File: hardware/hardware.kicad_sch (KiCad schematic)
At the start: 0 parts

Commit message: Prel. pin assignments for base station
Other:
- sheet GNSS ports: added 3V3, GND, RXD, SCL, SDA, TXD; removed none
- sheet Heltecv3 ports: added 3V3, 5V, GND, SCL, SDA, UART_RX, UART_TX; removed none

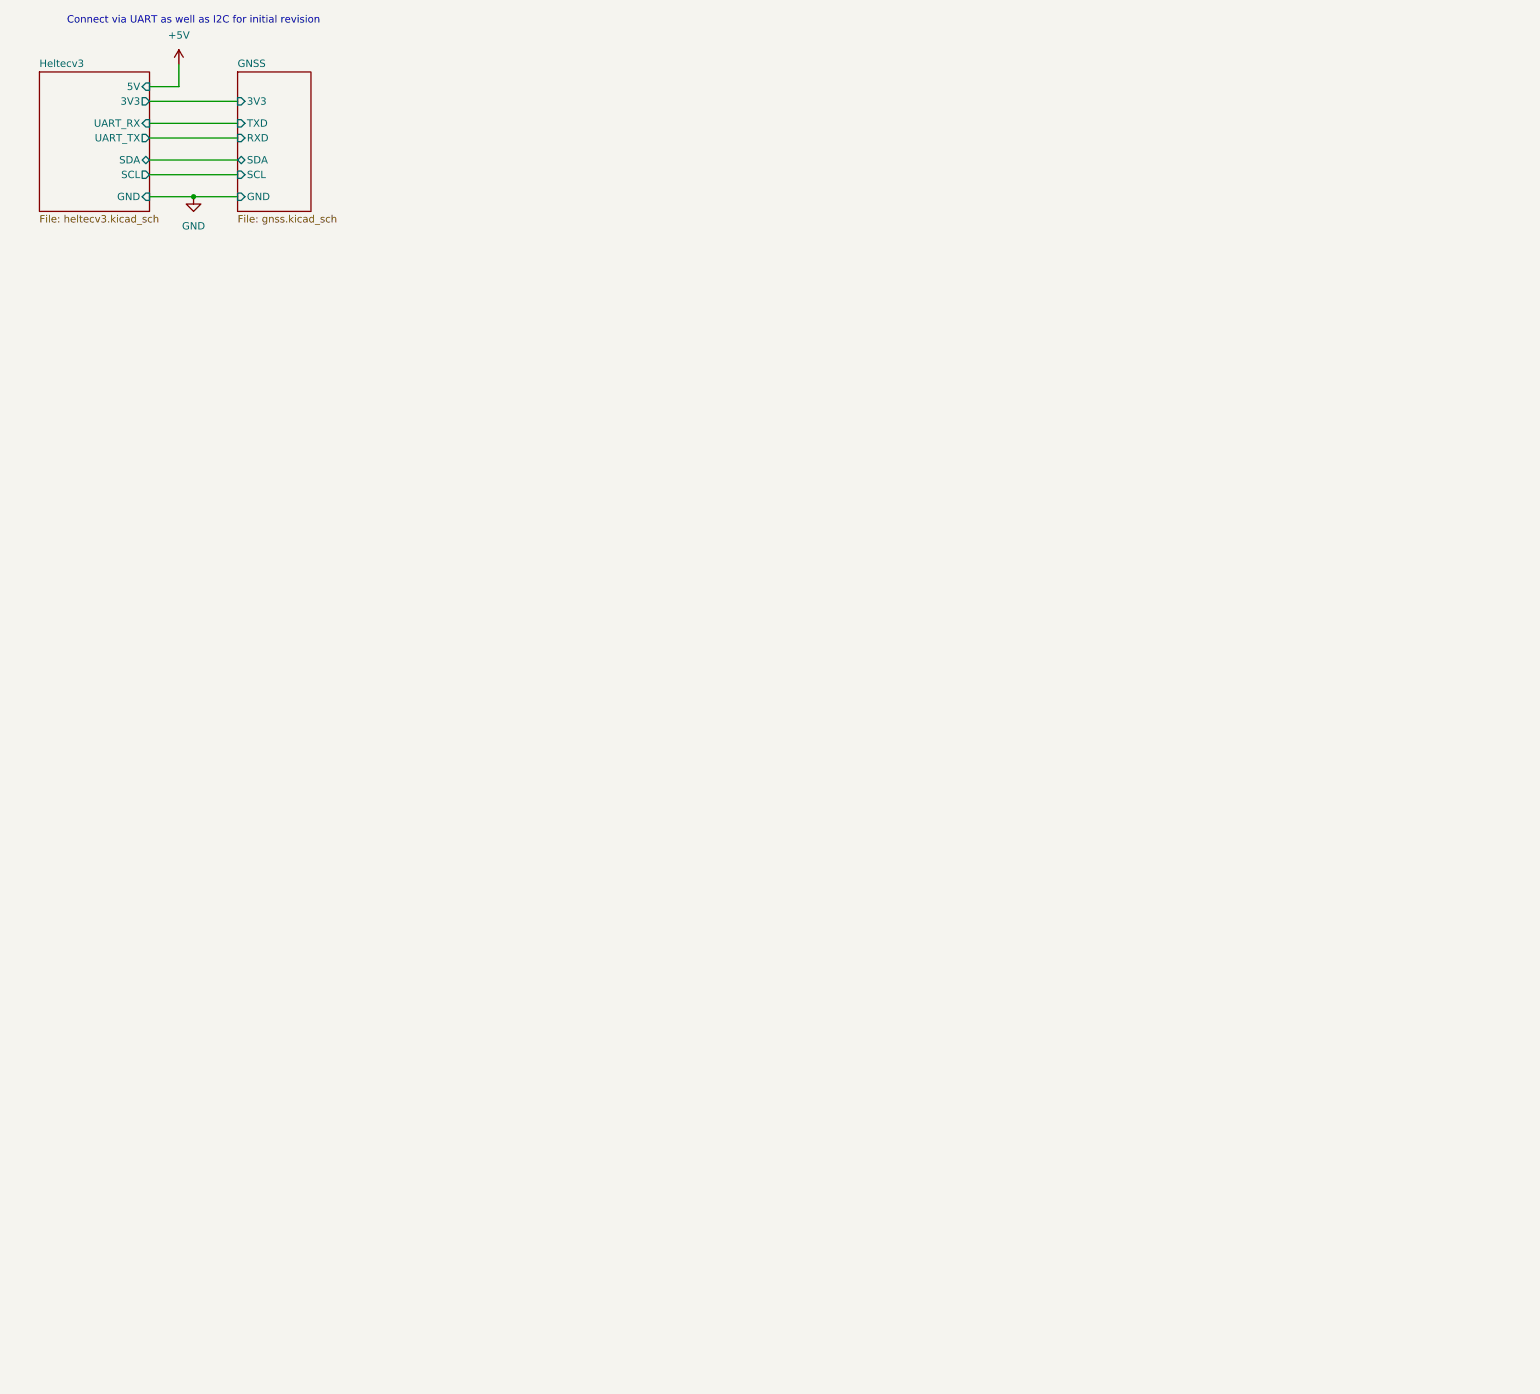
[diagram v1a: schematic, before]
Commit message: added footprints, symbols and so on. also added esp32 to main schematic
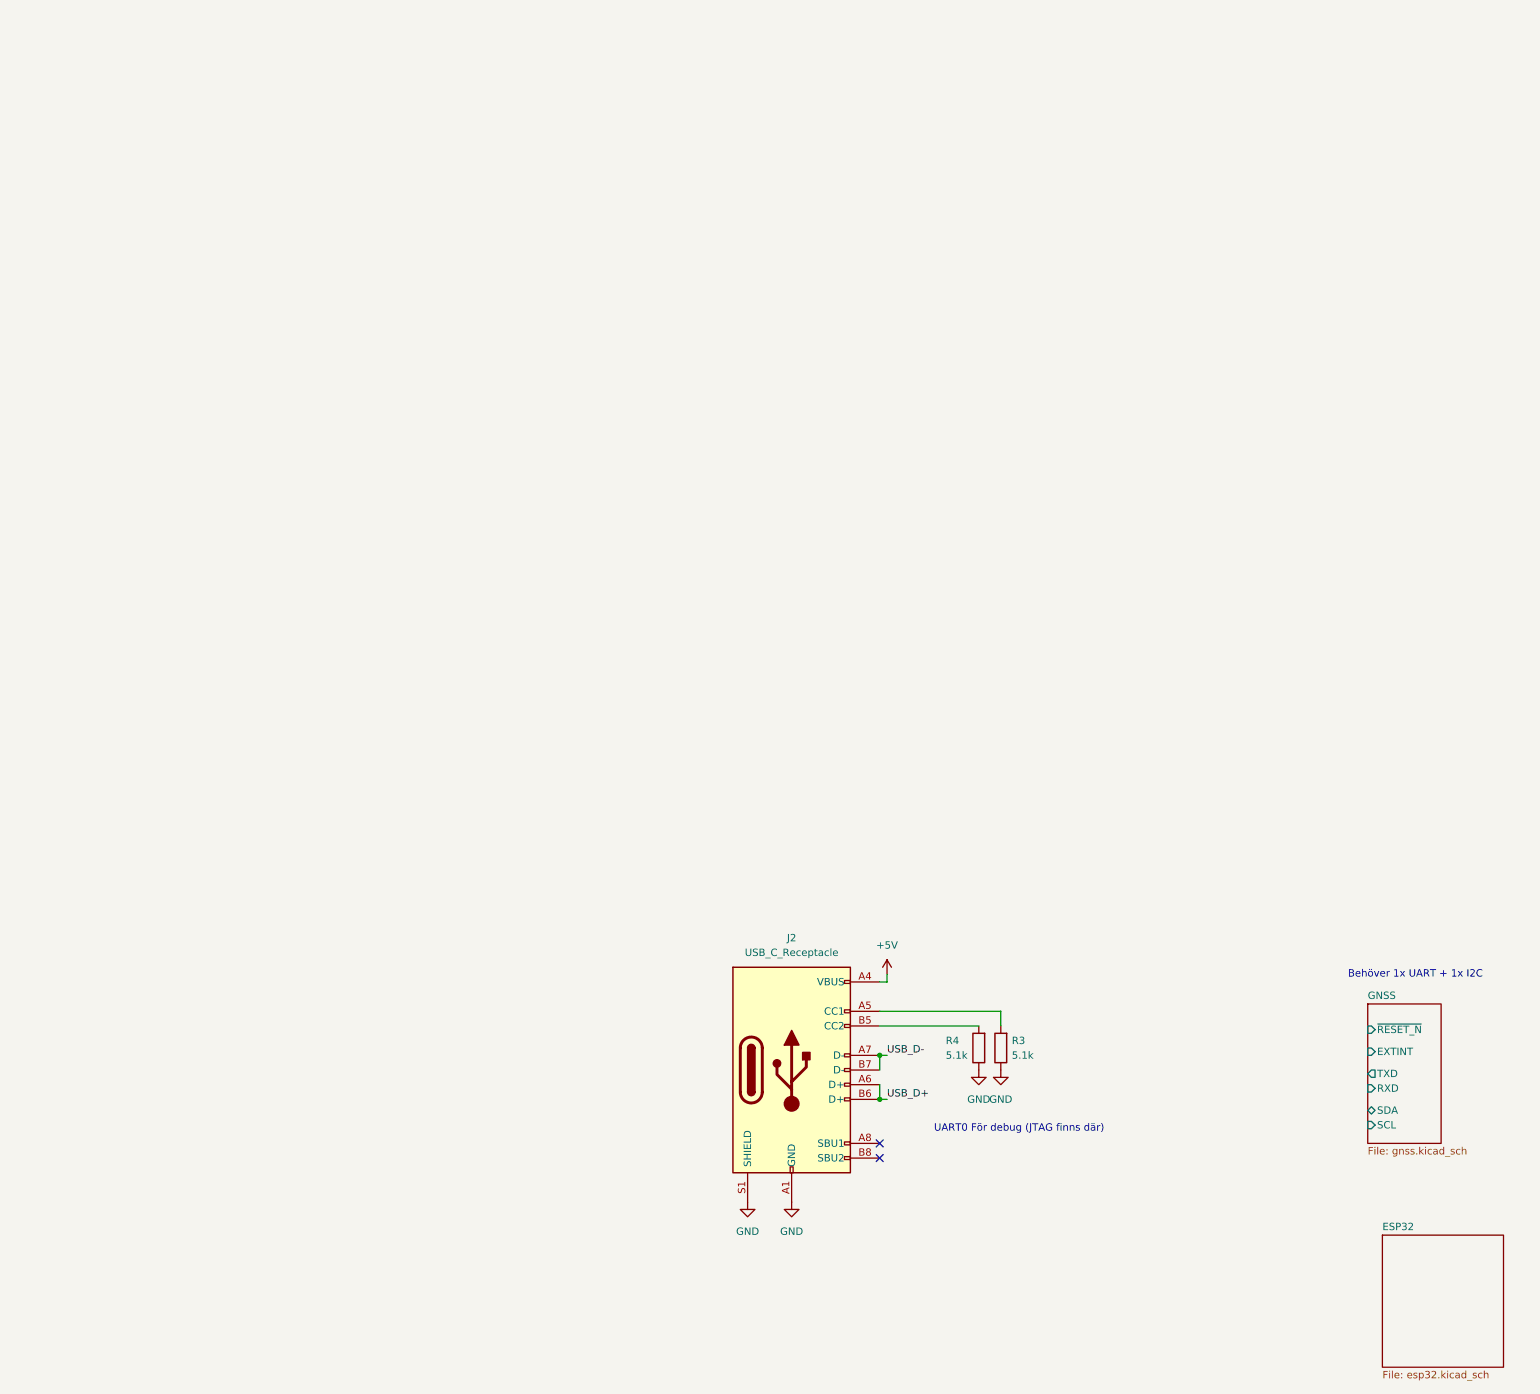
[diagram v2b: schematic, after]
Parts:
- added J2: USB_C_Receptacle, symbol Connector:USB_C_Receptacle_USB2.0_16P
- added R3, R4: 5.1k, symbol Device:R
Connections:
- net +5V: now also J2.A4 (VBUS), J2.A9 (VBUS), J2.B4 (VBUS), J2.B9 (VBUS)
- net GND: now also J2.A1 (GND), J2.A12 (GND), J2.B1 (GND), J2.B12 (GND), J2.S1 (SHIELD), R3.1, R4.1
- new net: J2.B5 (CC2), R4.2
- new net: J2.A5 (CC1), R3.2
- new net USB_D+: J2.A6 (D+), J2.B6 (D+)
- new net USB_D-: J2.A7 (D-), J2.B7 (D-)
- no-connect marks 0 -> 2
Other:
- removed sheet Heltecv3
- added sheet ESP32 (esp32.kicad_sch)
- sheet GNSS ports: added EXTINT, ~{RESET_N}; removed 3V3, GND
- note added: "Behöver 1x UART + 1x I2C"
- note added: "UART0 För debug (JTAG finns där)"
- note removed: "Connect via UART as well as I2C for initial revision"
